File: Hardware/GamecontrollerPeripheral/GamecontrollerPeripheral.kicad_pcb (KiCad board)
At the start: 2 copper layers, 3 parts, among them J2 UPDI, U1 ATtiny1604-SS

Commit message: GamecontrollerPeripheral progres
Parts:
- added H1: MountingHole_Pad, MountingHole:MountingHole_2.2mm_M2_DIN965_Pad, F.Cu at (90.7, 84.8)
- added H2: MountingHole_Pad, MountingHole:MountingHole_2.2mm_M2_DIN965_Pad, F.Cu at (84.6, 123.7)
- added JP1: SDA_TOP, Jumper:SolderJumper-2_P1.3mm_Open_RoundedPad1.0x1.5mm, F.Cu at (166.1, 106.7)
- added JP2: SDA_BOT, Jumper:SolderJumper-2_P1.3mm_Open_RoundedPad1.0x1.5mm, B.Cu at (166.1, 106.7)
- added JP3: SCL_TOP, Jumper:SolderJumper-2_P1.3mm_Open_RoundedPad1.0x1.5mm, F.Cu at (166.1, 109.2)
- added JP4: SDA_BOT, Jumper:SolderJumper-2_P1.3mm_Open_RoundedPad1.0x1.5mm, B.Cu at (166.1, 109.2)
- added SW1: Joystick, InputDevices:Joystick-Universal, F.Cu at (72.8, 84.9)
- added SW6: DPad, InputDevices:D-Pad, F.Cu at (97.3, 110.7)
- moved Per1 8.38 mm to (172.6, 108.1)
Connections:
- Per1 pad 5: SDA -> Net-(JP1-A)
- Per1 pad 6: SCL -> Net-(JP2-A)

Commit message: GamecontrollerPeripheral progres
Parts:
- added C1: 0.1uF, Capacitor_SMD:C_0805_2012Metric_Pad1.18x1.45mm_HandSolder, F.Cu at (-14.6, -1.76)
- added D1: LED, LED_SMD:LED_0805_2012Metric_Pad1.15x1.40mm_HandSolder, F.Cu at (0.01, 4.19)
- added R1: 10K, Resistor_SMD:R_0805_2012Metric_Pad1.20x1.40mm_HandSolder, F.Cu at (-10.8, -1.76)
- added R2: 1K, Resistor_SMD:R_0805_2012Metric_Pad1.20x1.40mm_HandSolder, F.Cu at (-3.81, 4.19)
- moved H1 203.6 mm to (-81.9, -23.2)
- moved H2 203.6 mm to (-88.0, 15.6)
- moved Per1 203.6 mm to (0.00, 0.00)
- moved JP1 203.5 mm to (-6.35, -1.40)
- moved JP2 203.5 mm to (-6.35, -1.40)
- moved JP3 203.5 mm to (-6.35, 1.14)
- moved JP4 203.5 mm to (-6.35, 1.14)
- moved J2 201.7 mm to (-15.1, -4.70), turned to 90 degrees
- moved U1 191.0 mm to (-12.8, 3.94)
- moved SW6 154.1 mm to (-33.7, 29.7)
- moved SW1 143.3 mm to (-45.6, 4.19)
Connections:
- SW1 pad 2: unconnected-(SW1-X-C-Pad2) -> Joystick_X
- SW1 pad 5: unconnected-(SW1-Y-C-Pad5) -> Joystick_Y
- SW6 pad 1: unconnected-(SW6-A-Pad1) -> DPad_A
- SW6 pad 2: unconnected-(SW6-B-Pad2) -> DPad_B
- SW6 pad 3: unconnected-(SW6-C-Pad3) -> DPad_C
- SW6 pad 4: unconnected-(SW6-D-Pad4) -> DPad_D
- U1 pad 11: unconnected-(U1-PA1-Pad11) -> Net-(U1-PA1)
- U1 pad 12: unconnected-(U1-PA2-Pad12) -> Joystick_X
- U1 pad 13: unconnected-(U1-PA3-Pad13) -> Joystick_Y
- U1 pad 2: unconnected-(U1-PA4-Pad2) -> DPad_A
- U1 pad 3: unconnected-(U1-PA5-Pad3) -> DPad_B
- U1 pad 4: unconnected-(U1-PA6-Pad4) -> DPad_C
- U1 pad 5: unconnected-(U1-PA7-Pad5) -> DPad_D
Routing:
- net +3.3V: track 0.00 -> 38.1 mm, vias 0 -> 1
- net GND: track 0.00 -> 28.9 mm, vias 0 -> 1
- net Net-(JP2-A): track 0.00 -> 27.1 mm
- net SDA: track 0.00 -> 14.1 mm, vias 0 -> 1
- net UPDI_DATA: track 0.00 -> 13.2 mm, vias 0 -> 1
- net Joystick_Y: track 0.00 -> 12.5 mm
- net Joystick_X: track 0.00 -> 12.4 mm
- net Net-(JP1-A): track 0.00 -> 11.4 mm
- net SCL: track 0.00 -> 8.29 mm, vias 0 -> 1
- net Net-(U1-PA1): track 0.00 -> 5.08 mm, vias 0 -> 2
- net Net-(D1-K): track 0.00 -> 1.79 mm
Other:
- board outline added: 74.3 x 75.4 mm

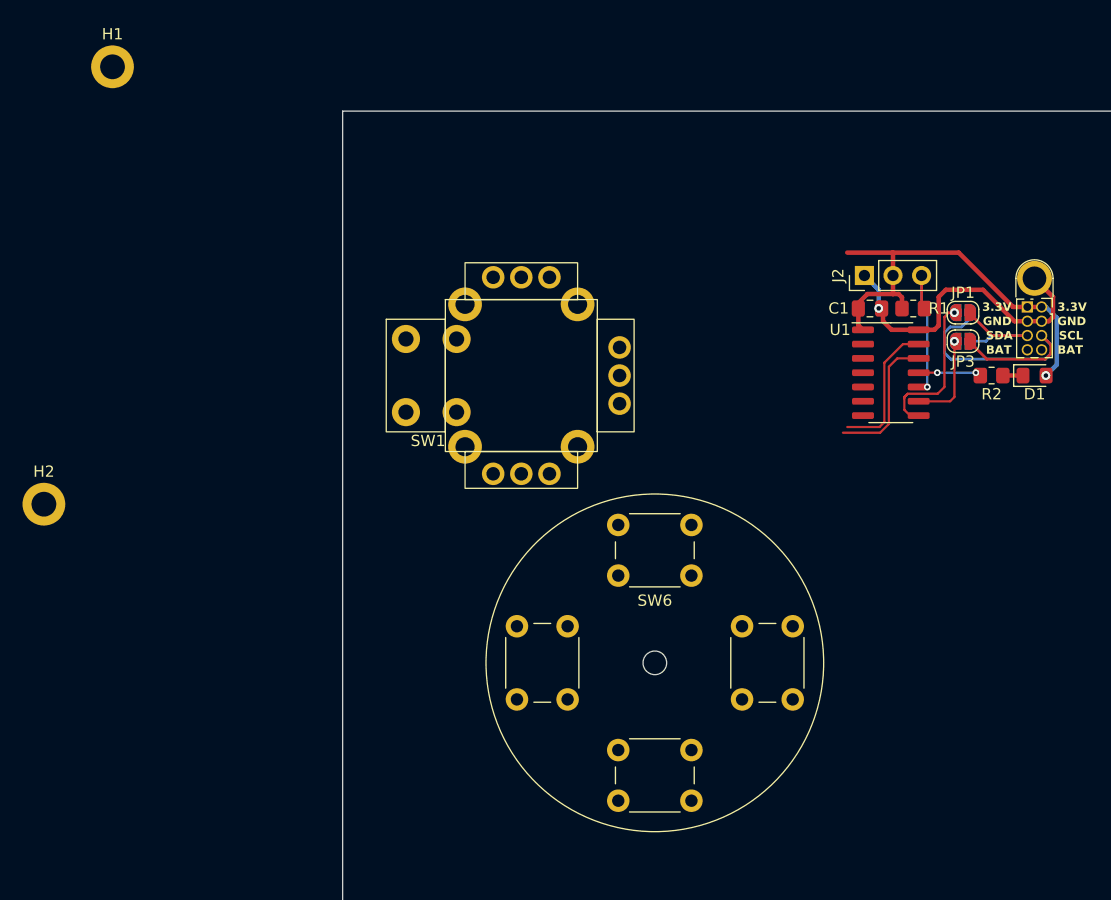
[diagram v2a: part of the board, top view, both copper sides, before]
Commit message: Need to make more commits; Changed design to use horizontal peripheral connectors. Changed models, more compact design. Still in progress
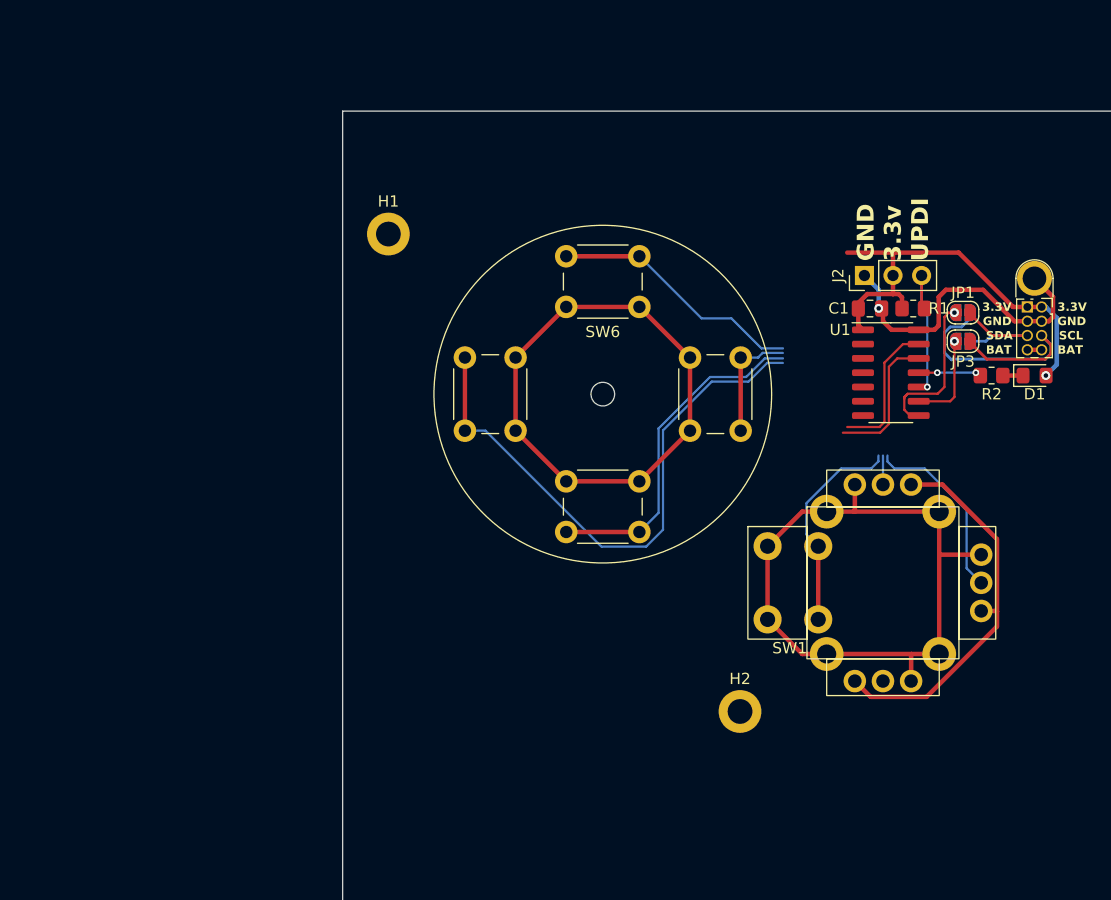
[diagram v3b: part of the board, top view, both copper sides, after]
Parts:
- moved H2 64.5 mm to (-26.2, 34.0)
- moved SW1 37.0 mm to (-13.5, 22.6)
- moved H1 28.7 mm to (-57.4, -8.38)
- moved SW6 24.3 mm to (-38.4, 5.84)
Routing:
- net GND: track 28.9 -> 141.2 mm
- net DPad_D: track 0.00 -> 51.0 mm
- net +3.3V: track 38.1 -> 72.7 mm
- net DPad_C: track 0.00 -> 30.0 mm
- net DPad_A: track 0.00 -> 22.6 mm
- net unconnected-(SW1-SW-A-Pad7): track 0.00 -> 19.2 mm
- net Joystick_Y: track 12.5 -> 28.8 mm
- net DPad_B: track 0.00 -> 10.4 mm
- net Joystick_X: track 12.4 -> 15.0 mm
- net +BATT: track 0.00 -> 1.27 mm
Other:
- board text added: "GND 3.3v UPDI"
